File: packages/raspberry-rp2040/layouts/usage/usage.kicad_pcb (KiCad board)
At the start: 4 copper layers, 36 parts

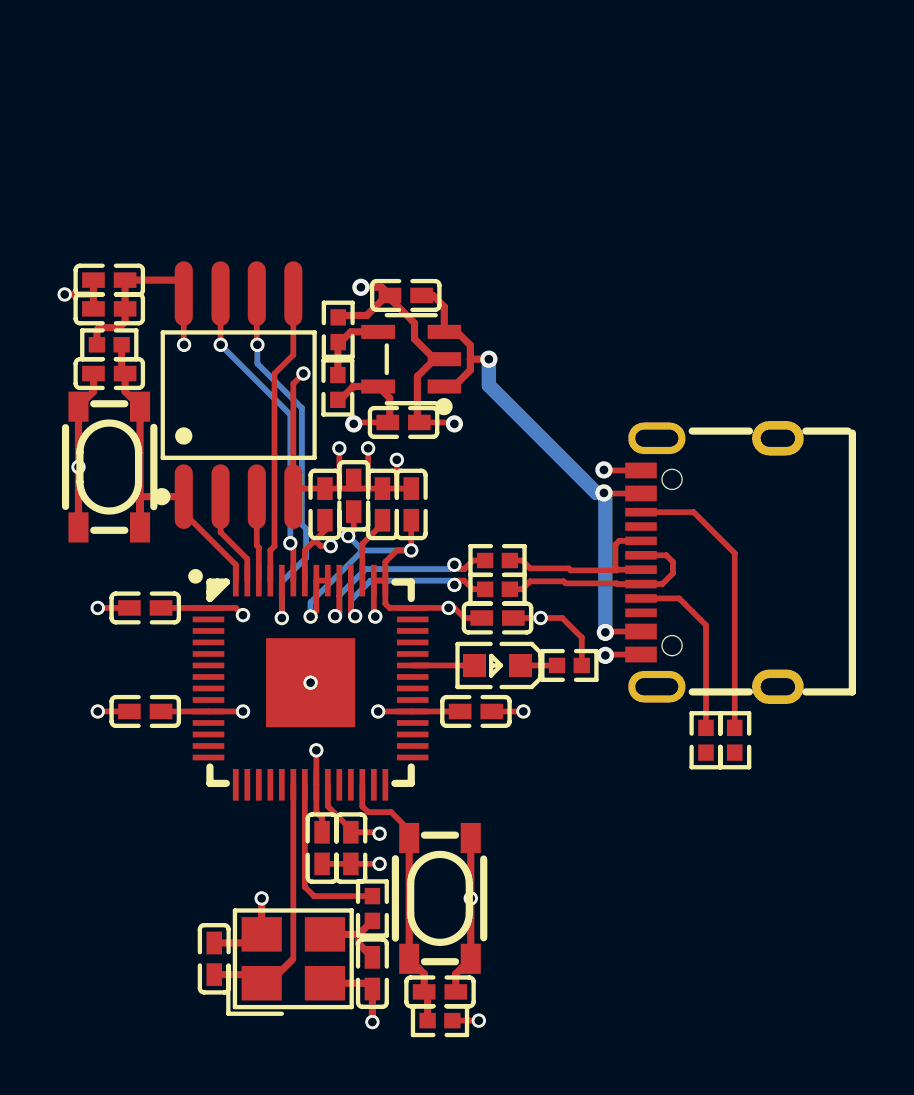
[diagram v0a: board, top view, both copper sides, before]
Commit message: fix docstrings, rename example > usage
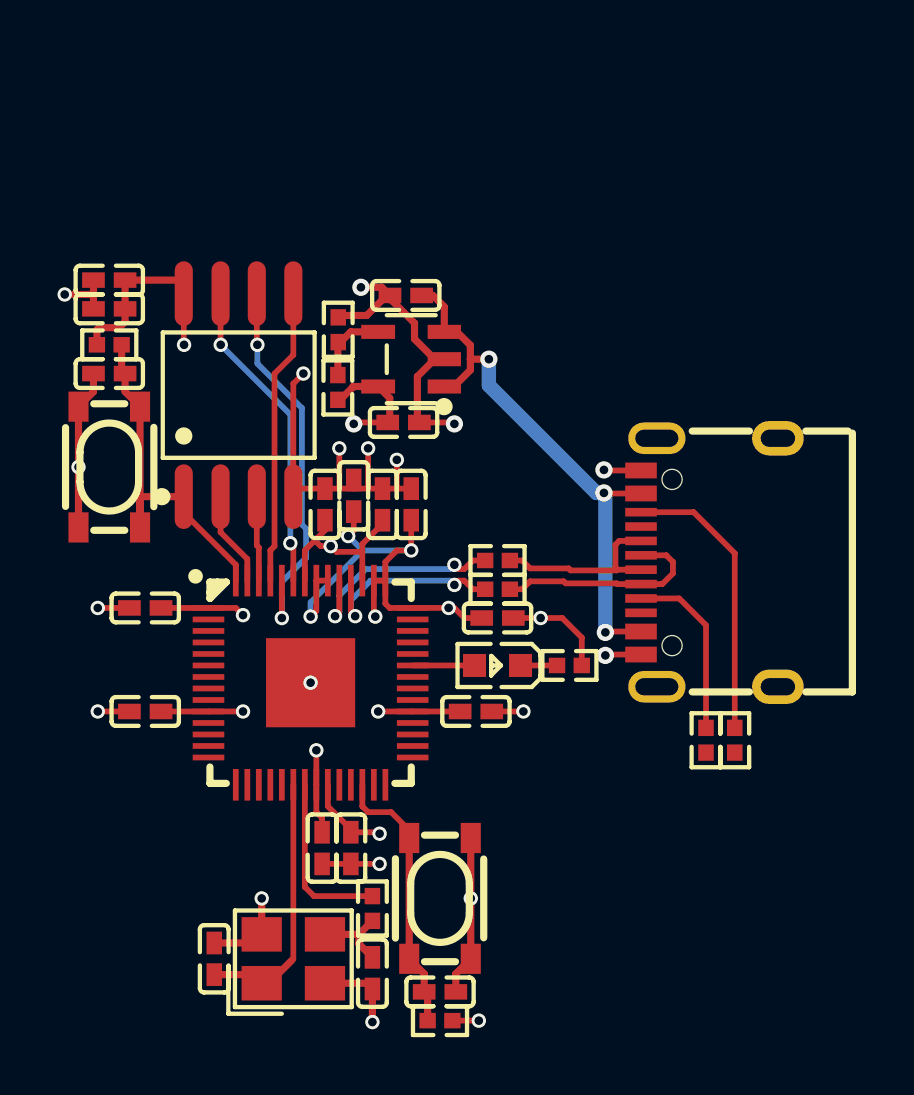
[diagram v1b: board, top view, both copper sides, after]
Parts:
- C7, C8: footprint YAGEO_CC0402JRNPO9BN150:C0402 -> FH_0402CG150J500NT:C0402
- R7, R8: footprint YAGEO_RC0402FR_0727RL:R0402 -> UNI_ROYAL_0402WGF270JTCE:R0402
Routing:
- net DVDD: track 20.7 -> 21.9 mm

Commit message: update regulator dependency
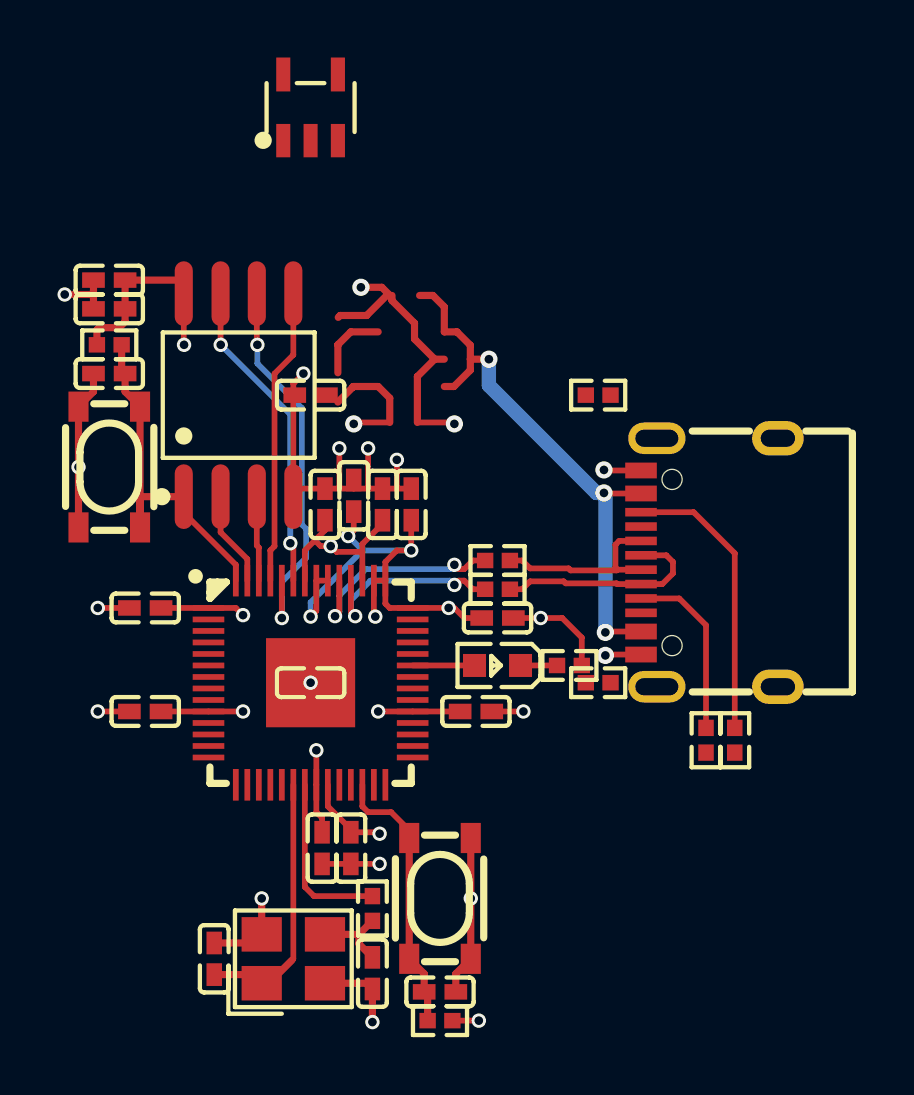
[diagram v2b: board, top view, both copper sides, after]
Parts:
- R1: value 5.1kΩ ±1% 62.5mW -> 10kΩ ±1% 62.5mW; footprint UNI_ROYAL_0402WGF5101TCE:R0402 -> UNI_ROYAL_0402WGF1002TCE:R0402
- R2: value 10kΩ ±1% 62.5mW -> 20kΩ ±1% 62.5mW; footprint UNI_ROYAL_0402WGF1002TCE:R0402 -> UNI_ROYAL_0402WGF2002TCE:R0402
- R7, R8: footprint UNI_ROYAL_0402WGF270JTCE:R0402 -> YAGEO_RC0402FR_0727RL:R0402
- U1: footprint ST_LDK220M_R:SOT-23-5_L3.0-W1.7-P0.95-LS2.8-BL -> STMicroelectronics_LDK220M_R:SOT-23-5_L3.0-W1.7-P0.95-LS2.8-BL
- moved R1 15.2 mm to (10.0, 0.00), turned to 0 degrees
- moved C1 13.9 mm to (0.00, 0.00), turned to 0 degrees
- moved U1 9.42 mm to (0.00, -20.0), turned to 0 degrees
- moved R2 9.06 mm to (10.0, -10.0), turned to 0 degrees
- moved C2 3.37 mm to (0.00, -10.0)
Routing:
- net (no net): track 0.00 -> 22.1 mm, vias 0 -> 3
- net hv: track 19.5 -> 0.00 mm, vias 3 -> 0
- net ADJ_NC: track 2.56 -> 0.00 mm

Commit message: update usage
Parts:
- R1: value 10kΩ ±1% 62.5mW -> 5.1kΩ ±1% 62.5mW; footprint UNI_ROYAL_0402WGF1002TCE:R0402 -> UNI_ROYAL_0402WGF5101TCE:R0402
- R2: value 20kΩ ±1% 62.5mW -> 10kΩ ±1% 62.5mW; footprint UNI_ROYAL_0402WGF2002TCE:R0402 -> UNI_ROYAL_0402WGF1002TCE:R0402
- R7, R8: footprint YAGEO_RC0402FR_0727RL:R0402 -> UNI_ROYAL_0402WGF270JTCE:R0402
- moved R1 15.2 mm to (0.79, -12.1), turned to 90 degrees
- moved C1 13.6 mm to (3.06, -13.3), turned to 180 degrees
- moved U1 9.54 mm to (3.32, -11.1), turned to 90 degrees
- moved R2 9.23 mm to (0.77, -10.1), turned to 90 degrees
- moved C2 3.20 mm to (2.99, -8.85)
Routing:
- net (no net): track 22.1 -> 0.00 mm, vias 3 -> 0
- net hv: track 0.00 -> 19.7 mm, vias 0 -> 3
- net ADJ_NC: track 0.00 -> 2.69 mm
